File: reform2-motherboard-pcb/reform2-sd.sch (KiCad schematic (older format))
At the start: 10 parts, among them J3 SD_Card, U8 TXS0108EPW

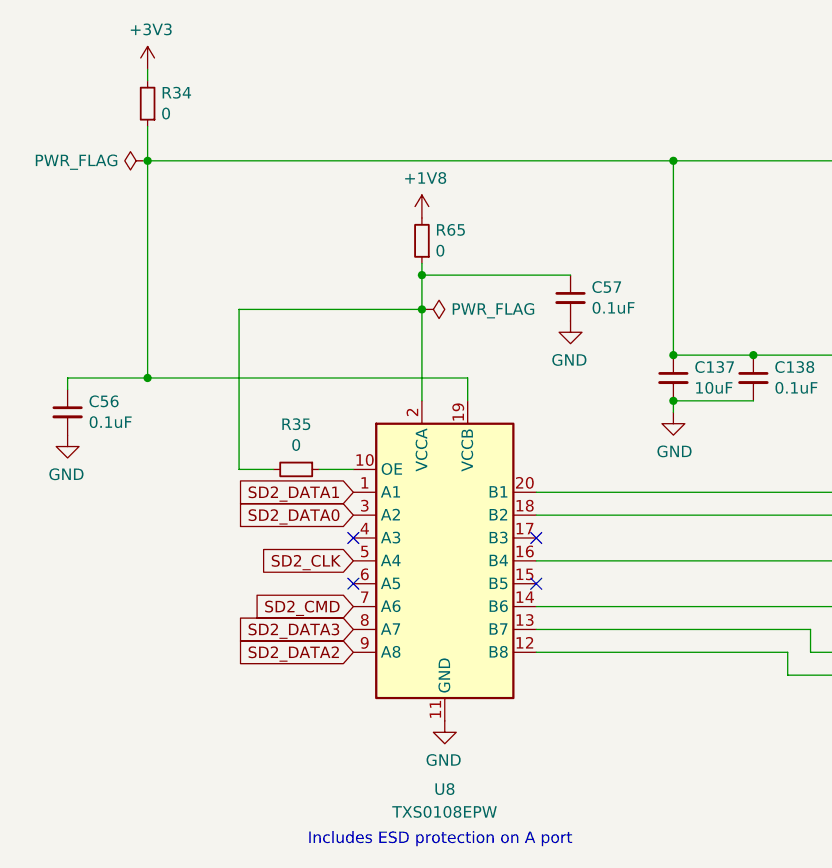
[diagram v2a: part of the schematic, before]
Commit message: reform2-motherboard: first R-1 snapshot. main changes: EMI, ESD, audio filter, enable FETs, SHDN fix, more rail switches
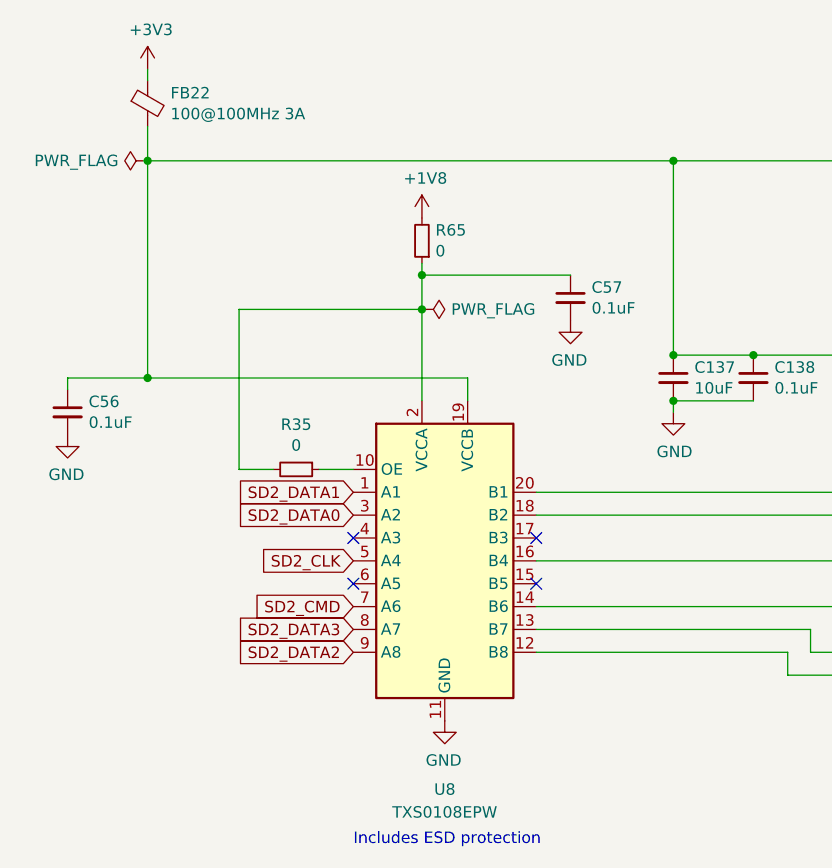
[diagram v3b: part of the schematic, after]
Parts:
- removed R34: 0, Resistor_SMD:R_0603_1608Metric, symbol Device:R_Small
- added FB22: 100@100MHz 3A, Inductor_SMD:L_0603_1608Metric, symbol Device:Ferrite_Bead_Small
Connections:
- net +3V3: now also FB22.1
- net at C137.1, C138.1, C56.1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: now also FB22.2
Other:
- note added: "Includes ESD protection"
- note removed: "Includes ESD protection on A port"
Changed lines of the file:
@@
 Wire Wire Line
 	7950 3950 7950 3850
-Text Notes 3400 5200 0    50   ~ 0
-Includes ESD protection on A port
+Text Notes 3600 5200 0    50   ~ 0
+Includes ESD protection
 Text Notes 6600 4900 0    50   ~ 0
 TE 1775059-1
@@
 Wire Wire Line
 	3900 2700 3900 2850
-$Comp
-L Device:R_Small R34
-U 1 1 5E9353CA
-P 2700 1950
-F 0 "R34" H 2641 1904 50  0000 R CNN
-F 1 "0" H 2641 1995 50  0000 R CNN
-F 2 "Resistor_SMD:R_0603_1608Metric" H 2700 1950 50  0001 C CNN
-F 3 "~" H 2700 1950 50  0001 C CNN
-F 4 "Vishay Dale" H 2700 1950 50  0001 C CNN "Manufacturer"
-F 5 "CRCW06030000Z0EAC" H 2700 1950 50  0001 C CNN "Manufacturer_No"
-F 6 "Mouser" H 2700 1950 50  0001 C CNN "Distributor"
-F 7 "y" H 2700 1950 50  0001 C CNN "Checked"
-	1    2700 1950
-	-1   0    0    1
-$EndComp
 Wire Wire Line
 	2700 1850 2700 1800
@@
 Wire Wire Line
 	3100 2850 3900 2850
+$Comp
+L Device:Ferrite_Bead_Small FB?
+U 1 1 60257C6A
+P 2700 1950
+AR Path="/5D06AC46/60257C6A" Ref="FB?"  Part="1"
+AR Path="/5D0CA3EB/60257C6A" Ref="FB22"  Part="1"
+F 0 "FB22" H 2800 1996 50  0000 L CNN
+F 1 "100@100MHz 3A" H 2800 1905 50  0000 L CNN
+F 2 "Inductor_SMD:L_0603_1608Metric" V 2630 1950 50  0001 C CNN
+F 3 "~" H 2700 1950 50  0001 C CNN
+F 4 "Murata" H 2700 1950 50  0001 C CNN "Manufacturer"
+F 5 "BLM18KG101TN1D" H 2700 1950 50  0001 C CNN "Manufacturer_No"
+F 6 "y" H 2700 1950 50  0001 C CNN "Checked"
+F 7 "Mouser" H 2700 1950 50  0001 C CNN "Distributor"
+	1    2700 1950
+	1    0    0    -1
+$EndComp
 $EndSCHEMATC

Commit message: reform2-motherboard: schematics,PCB,BOM,models for R-2C (probably final)
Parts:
- added C168, C169: 0.1uF, Capacitor_SMD:C_0603_1608Metric, symbol Device:C_Small
- added U28: SN74AVC1T45, Package_TO_SOT_SMD:SOT-23-6, symbol reform2:SN74AVC1T45
- R35: value 0 -> 1.5k; Manufacturer Vishay Dale -> Yageo; Manufacturer_No CRCW06030000Z0EAC -> RC0603FR-071K5L
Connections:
- net GND: now also C168.2, C169.2, U28.2 (GND)
- net SD2_CLK: now also U28.3 (A); no longer U8.5 (A4)
- net at C137.1, C138.1, C56.1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: now also C169.1, U28.6 (VCCB)
- net at J3.5 (CLK): now also U28.4 (B); no longer U8.16 (B4)
- net at C57.1, R65.1, U8.2 (VCCA): now also R35.1, C168.1, U28.1 (VCCA); no longer R35.2
- net at U8.10 (OE): now also R35.2, U28.5 (DIR); no longer R35.1
- no-connect marks 5 -> 7
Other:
- moved on the sheet: C137, C138, C56, C57, FB22, R65, U8
